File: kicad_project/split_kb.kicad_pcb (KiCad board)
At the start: 2 copper layers, 171 x 137.6 mm, 99 parts, among them J1 4P4C, J2 Conn_01x04_Socket, J3 4P4C, J4 Conn_01x04_Pin

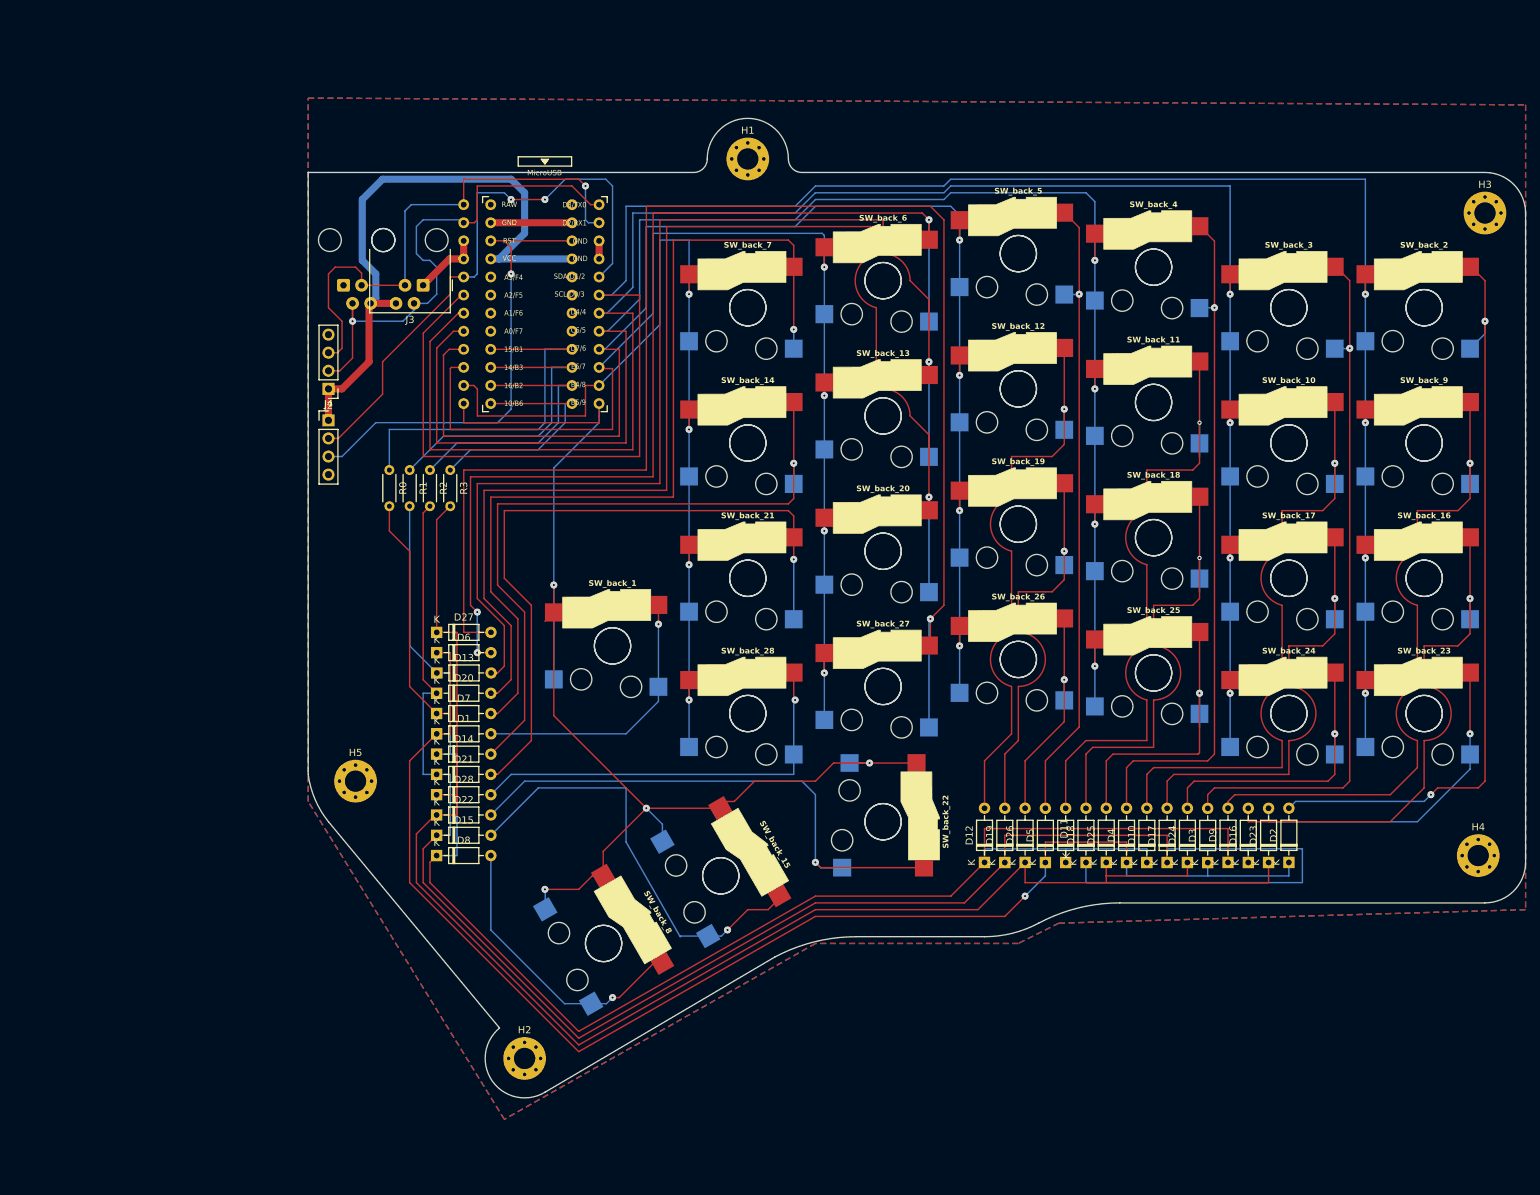
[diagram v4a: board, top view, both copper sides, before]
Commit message: Grounded EN pin, moved a mounting hole
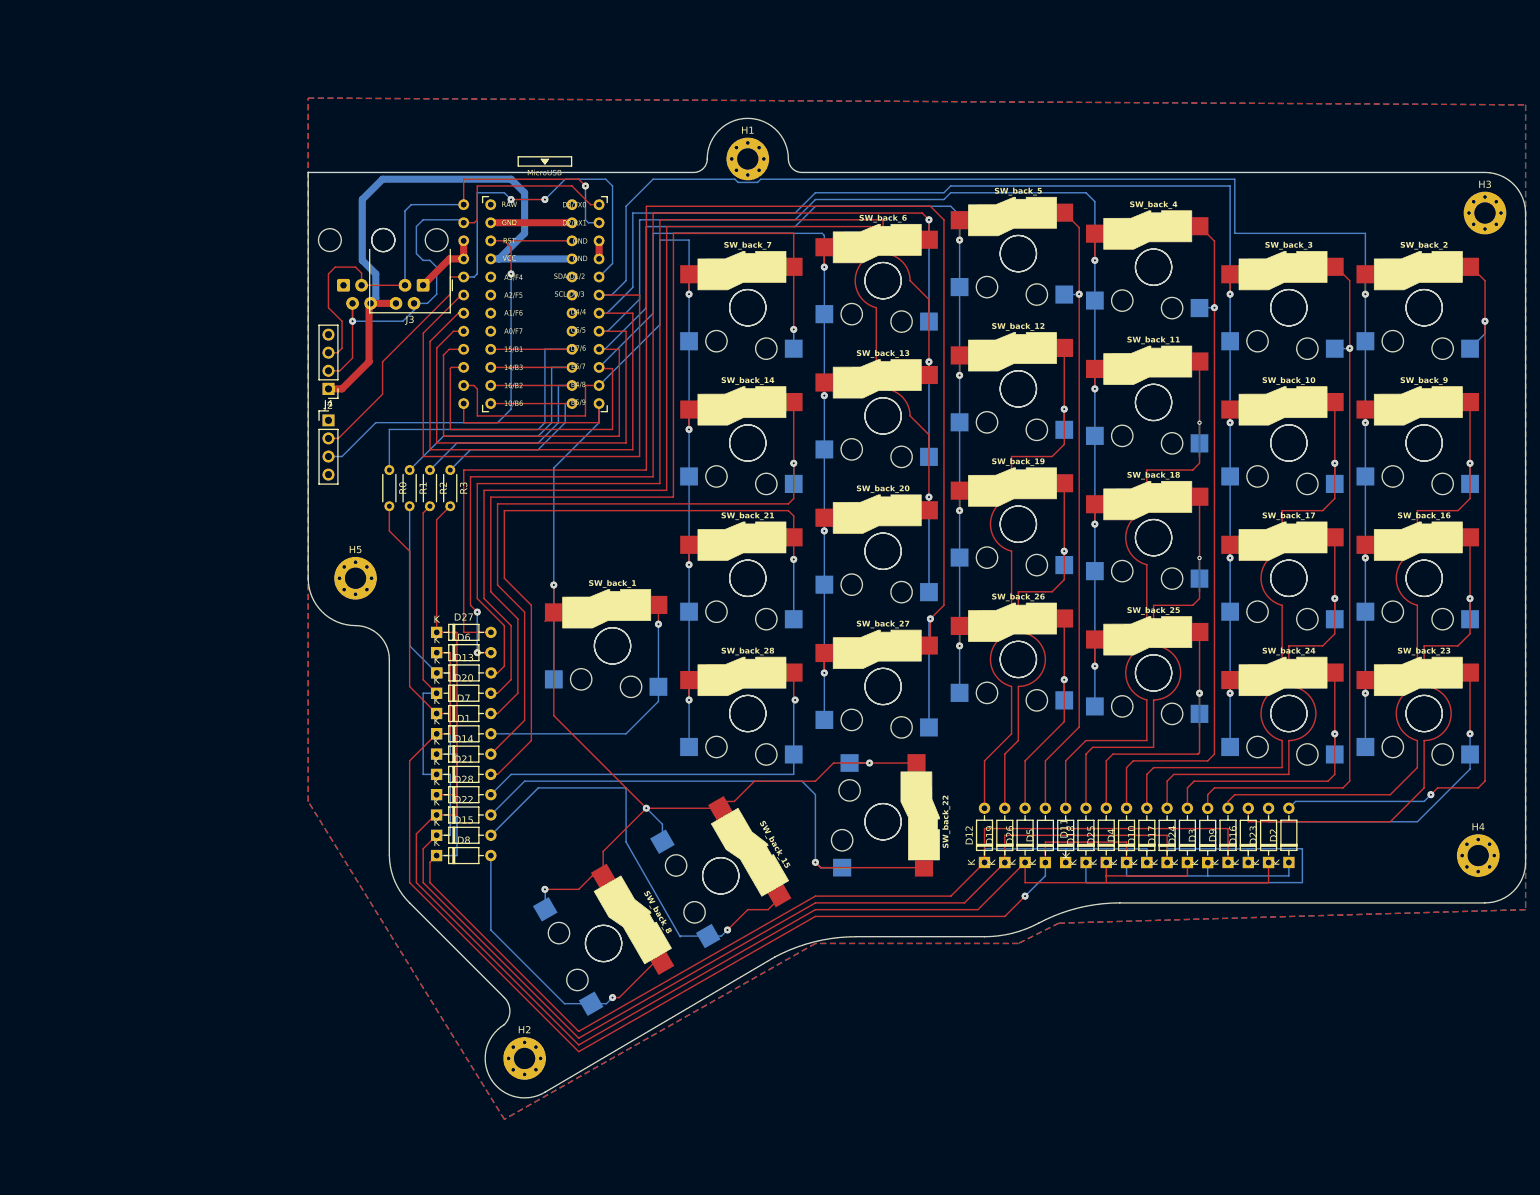
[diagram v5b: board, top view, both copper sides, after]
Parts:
- moved H5 28.5 mm to (73.2, 95.0)
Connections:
- J4 pad 1: VCC -> GND
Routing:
- net VCC: track 86.2 -> 81.8 mm
- net Net-(D7-A): track 127.6 -> 129.9 mm
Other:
- outline, holes or cut-outs redrawn
